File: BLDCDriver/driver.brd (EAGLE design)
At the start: 160 x 100 mm, 39 parts, among them Q1 NJM7800S, U1 QFN50P400X400X100-25NDRV8300D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, U2 AS5048A-HTSP-500, U4 SOP80P620X125-8N

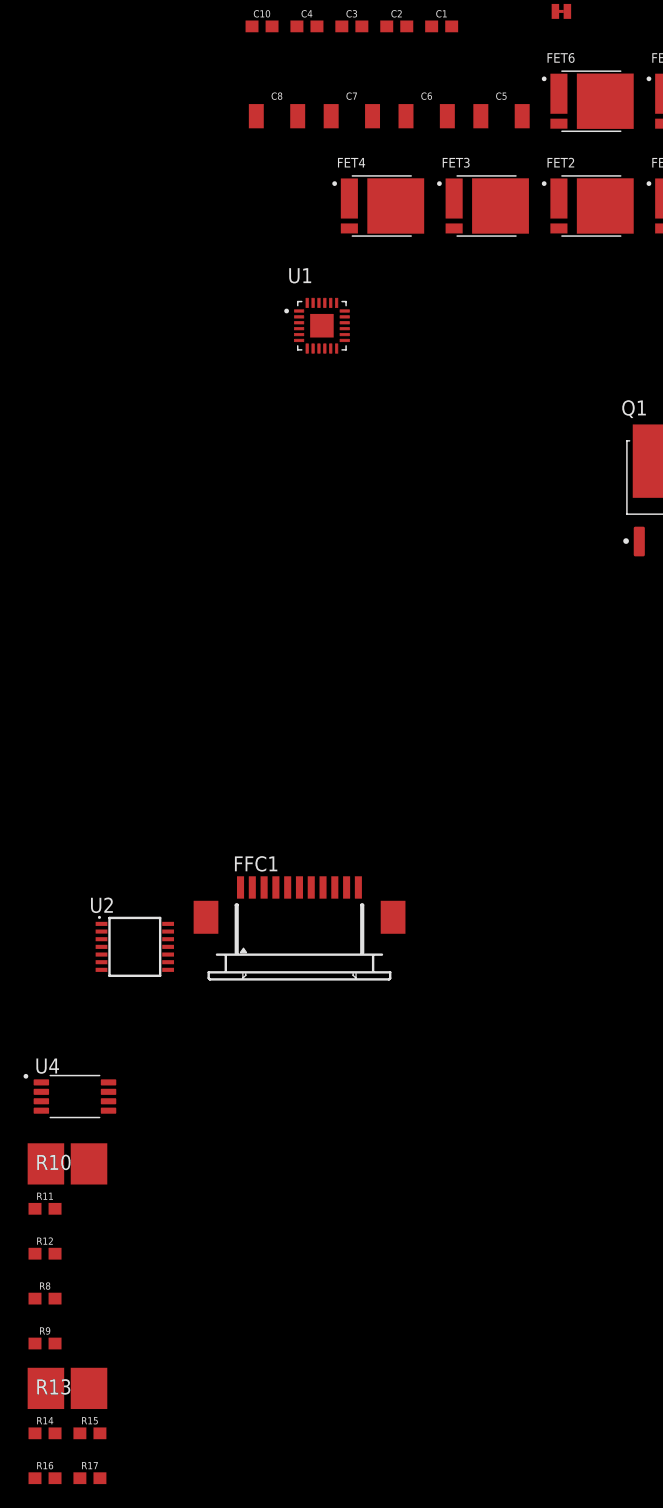
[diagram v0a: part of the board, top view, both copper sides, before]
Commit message: STM32と磁気エンコーダを追加した
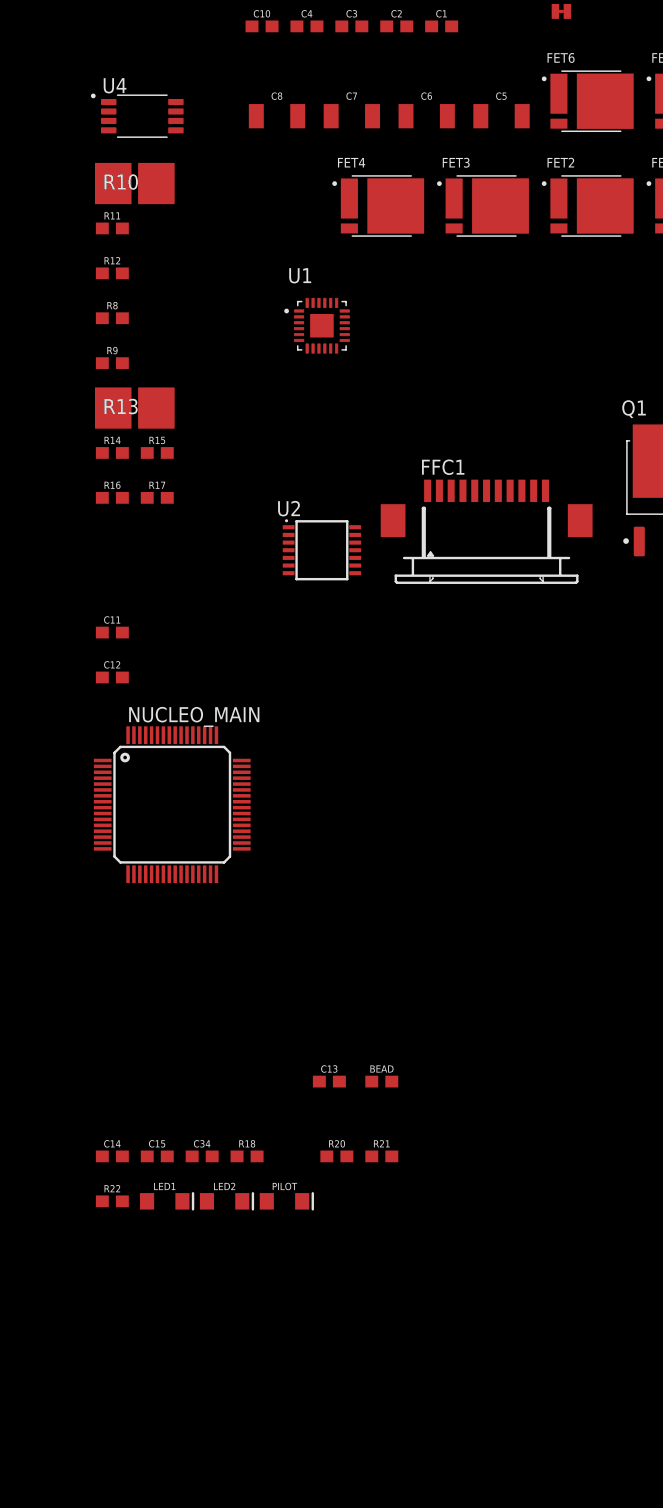
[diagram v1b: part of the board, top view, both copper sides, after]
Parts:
- added BEAD: 0, SparkFun-Resistors:0603
- added C11, C12, C15, C34: 0.1uF, SparkFun-Capacitors:0603
- added C13: 0.1UF_1608, Custom_Designed_By_Yusei:1608
- added C14: 4.7uF, SparkFun-Capacitors:0603
- added LED1, LED2, PILOT: (no value), Custom_Designed_By_Yusei:LED-1206
- added NUCLEO_MAIN: F446RET6, STM32F446RET6:STM32F446RET6
- added R18: 10k, Custom_Designed_By_Yusei:R0603
- added R20, R21, R22: 1k, Custom_Designed_By_Yusei:R0603
- moved R10 83.4 mm to (-64.1, 34.9)
- moved R11 83.4 mm to (-66.0, 31.1)
- moved R12 83.4 mm to (-66.0, 27.3)
- moved R13 83.4 mm to (-64.1, 15.9)
- moved R14 83.4 mm to (-66.0, 12.1)
- moved R15 83.4 mm to (-62.2, 12.1)
- moved R16 83.4 mm to (-66.0, 8.26)
- moved R17 83.4 mm to (-62.2, 8.26)
- moved R8 83.4 mm to (-66.0, 23.5)
- moved R9 83.4 mm to (-66.0, 19.7)
- moved U4 83.4 mm to (-63.5, 40.6)
- moved FFC1 37.2 mm to (-34.3, 6.35)
- moved U2 37.2 mm to (-48.3, 3.81)
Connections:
- removed net VDD3V: U2.12
- new net BALLRX: NUCLEO_MAIN.PA3
- new net BOOT0: NUCLEO_MAIN.BOOT0, R18.2
- new net BUTTON_CENTER: NUCLEO_MAIN.PC14
- new net BUTTON_LEFT: NUCLEO_MAIN.PC15
- new net BUTTON_RIGHT: NUCLEO_MAIN.PC13
- new net CLK: U2.2
- new net CS: U2.1
- new net LED1: LED1.A
- new net LED2: LED2.A
- new net LINE_A0: NUCLEO_MAIN.PB12
- new net LINE_A1: NUCLEO_MAIN.PB13
- new net MISO: U2.3
- new net MOSI: U2.4
- new net N$12: LED2.C, R21.1
- new net N$13: LED1.C, R22.1
- new net NRST: C13.1, NUCLEO_MAIN.NRST
- new net POWERLED_RESISTOR: PILOT.A, R20.1
- new net RGB_B: NUCLEO_MAIN.PA12
- new net RGB_G: NUCLEO_MAIN.PA8
- new net RGB_R: NUCLEO_MAIN.PC9
- new net SWCLK: NUCLEO_MAIN.PA14
- new net SWDIO: NUCLEO_MAIN.PA13
- new net VCAP: C14.1, NUCLEO_MAIN.VCAP_1
- new net VDDA: BEAD.1, NUCLEO_MAIN.VREF+
- net 3V3: now also BEAD.2, C11.1, C12.1, C15.1, C34.1, NUCLEO_MAIN.VBAT, NUCLEO_MAIN.VDD, NUCLEO_MAIN.VDD1, NUCLEO_MAIN.VDD2, NUCLEO_MAIN.VDD3, R20.2, U2.12
- net GND: now also C11.2, C12.2, C13.2, C14.2, C15.2, C34.2, NUCLEO_MAIN.VREF-, NUCLEO_MAIN.VSS, NUCLEO_MAIN.VSS1, NUCLEO_MAIN.VSS2, NUCLEO_MAIN.VSS3, PILOT.C, R18.1, R21.2, R22.2, U2.13

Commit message: somefix
# ==== Emojis ====
# ✨ :sparkles: Add new feature
# ✅  :white_check_mark: Update existing feature (not bug)
# ⚠️  :warning: Fix bug/error
# 🔥  :fire: Remove files or features
# ✏️ :pencil2: Fix typos
# 📝  :memo: Update documentation
# ♻️  :recycle: Dependencies update
# 🐧  :penguin: Improved the Linux
# 🍎  :apple: Improved the macOS
# 🔖 :bookmark: Add new library
# 🎉  :tada: Initial commit

# ==== Format ====
# :emoji: Subject
#
# Commit body...

# ==== Messages ====
# 新規(ファイル)機能追加: Add
# 機能修正、既存機能追加（バグではない): Update
# リファクタリング: Clean
# ファイル名変更:
# 削除など: Remove
# バグ修正: Fix
# バージョンアップ: Upgrade
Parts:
- added C16: 22UF-1210, SparkFun-Capacitors:1210
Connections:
- net GND: now also C16.1
- net GVDD: now also C16.2
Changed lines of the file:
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@@
 <attribute name="VALUE" x="-64.624" y="-17.7501" size="1.27" layer="27"/>
+</element>
+<element name="C16" library="SparkFun-Capacitors" package="1210" value="22UF-1210" x="-64.77" y="-55.88" smashed="yes">
+<attribute name="NAME" x="-64.77" y="-54.483" size="0.6096" layer="25" font="vector" ratio="20" align="bottom-center"/>
+<attribute name="VALUE" x="-64.77" y="-57.277" size="0.6096" layer="27" font="vector" ratio="20" align="top-center"/>
 </element>
 </elements>
@@
 <contactref element="Q1" pad="G"/>
 <contactref element="C4" pad="2"/>
-<contactref element="C8" pad="1"/>
-<contactref element="C9" pad="1"/>
 <contactref element="C10" pad="2"/>
 <contactref element="R7" pad="1"/>
@@
 <contactref element="NUCLEO_MAIN" pad="VSS"/>
 <contactref element="NUCLEO_MAIN" pad="VREF-"/>
+<contactref element="C8" pad="1"/>
+<contactref element="C9" pad="1"/>
+<contactref element="C16" pad="1"/>
+<wire x1="-65.19" y1="-51.435" x2="-66.525" y2="-55.88" width="0" layer="19" extent="1-1"/>
 <wire x1="-65.19" y1="-47.625" x2="-65.19" y2="-51.435" width="0" layer="19" extent="1-1"/>
 <wire x1="-61.38" y1="-47.625" x2="-65.19" y2="-47.625" width="0" layer="19" extent="1-1"/>
@@
 <contactref element="C8" pad="2"/>
 <contactref element="C9" pad="2"/>
-<wire x1="-28.448" y1="49.53" x2="-14.755" y2="49.53" width="0" layer="19" extent="1-1"/>
-<wire x1="-50.38" y1="48.26" x2="-28.448" y2="49.53" width="0" layer="19" extent="1-1"/>
-<wire x1="-50.315" y1="40.64" x2="-50.38" y2="48.26" width="0" layer="19" extent="1-1"/>
-<wire x1="-50.195" y1="22.61" x2="-50.315" y2="40.64" width="0" layer="19" extent="1-1"/>
-<wire x1="-16.77" y1="4.55" x2="-50.195" y2="22.61" width="0" layer="19" extent="1-1"/>
+<contactref element="C16" pad="2"/>
+<wire x1="-16.77" y1="4.55" x2="-63.015" y2="-55.88" width="0" layer="19" extent="1-1"/>
+<wire x1="-50.195" y1="22.61" x2="-16.77" y2="4.55" width="0" layer="19" extent="1-1"/>
+<wire x1="-50.315" y1="40.64" x2="-50.195" y2="22.61" width="0" layer="19" extent="1-1"/>
+<wire x1="-50.38" y1="48.26" x2="-50.315" y2="40.64" width="0" layer="19" extent="1-1"/>
+<wire x1="-28.448" y1="49.53" x2="-50.38" y2="48.26" width="0" layer="19" extent="1-1"/>
+<wire x1="-14.755" y1="49.53" x2="-28.448" y2="49.53" width="0" layer="19" extent="1-1"/>
 </signal>
 <signal name="DT">

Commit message: 自分、泣いていいすか
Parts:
- added C17: 0.1uF, Custom_Designed_By_Yusei:1608
- added C18: (no value), cap-pan40:E3,5-8
- added D1, D3, D4, D5, D6: WHITE, SparkFun-LED:LED-0603
- added D2: RED, SparkFun-LED:LED-0603
- added R19, R24, R25: 10k, SparkFun-Resistors:0603
- added R23, R26: 7k, SparkFun-Resistors:0603
- added R27: 8k, SparkFun-Resistors:0603
- added S1: SKRPACE010, Alps SW:SW_SKRPACE010
- added STLINK: MAIN, jst-xh:B6B-XH-A
- added U$2: BAT, BAT:BAT
- moved C16 144.1 mm to (25.4, 56.5)
- moved C14 141.7 mm to (40.0, 46.4)
- moved LED1 141.7 mm to (44.5, 42.5)
- moved LED2 141.7 mm to (49.5, 42.5)
- moved PILOT 141.7 mm to (54.6, 42.5)
- moved R22 141.7 mm to (40.0, 42.5)
- moved C15 141.7 mm to (43.8, 46.4)
- moved C34 141.7 mm to (47.6, 46.4)
- moved R18 141.7 mm to (51.4, 46.4)
- moved BEAD 119.6 mm to (45.1, 39.4)
- moved C13 119.6 mm to (40.6, 39.4)
- moved R20 119.6 mm to (41.3, 33.0)
- moved R21 119.6 mm to (45.1, 33.0)
- moved C11 106.2 mm to (38.1, 17.8)
- moved C12 106.2 mm to (38.1, 14.0)
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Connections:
- net BALLRX renamed USBRX
- removed net BUTTON_CENTER: NUCLEO_MAIN.PC14
- removed net BUTTON_LEFT: NUCLEO_MAIN.PC15
- removed net BUTTON_RIGHT: NUCLEO_MAIN.PC13
- removed net LINE_A0: NUCLEO_MAIN.PB12
- removed net LINE_A1: NUCLEO_MAIN.PB13
- removed net RGB_B: NUCLEO_MAIN.PA12
- removed net RGB_G: NUCLEO_MAIN.PA8
- removed net RGB_R: NUCLEO_MAIN.PC9
- new net C_U: NUCLEO_MAIN.PA0, R16.1, U4.1
- new net LED: NUCLEO_MAIN.PC14, R23.2
- new net N$14: D1.A, R19.1
- new net N$15: D2.A, R27.1
- new net N$16: D3.A, R24.1
- new net N$17: D4.A, R25.1
- new net N$18: D5.A, R26.1
- new net N$21: D6.A, R23.1
- new net SW: NUCLEO_MAIN.PC13, S1.2
- new net USBTX: NUCLEO_MAIN.PA2, STLINK.1
- net 3V3: now also C17.1, STLINK.5
- net CLK: now also NUCLEO_MAIN.PA5
- net CS: now also NUCLEO_MAIN.PB6
- net C_V: now also NUCLEO_MAIN.PA1; no longer R16.1, U4.1
- net GND: now also C17.2, C18.-, D1.C, D2.C, D3.C, D4.C, D5.C, D6.C, S1.4, STLINK.6, U$2.G
- net GVDD: now also R27.2
- net INA: now also NUCLEO_MAIN.PC7
- net INB: now also NUCLEO_MAIN.PB4
- net INC: now also NUCLEO_MAIN.PB10
- net MISO: now also NUCLEO_MAIN.PA6
- net MOSI: now also NUCLEO_MAIN.PA7
- net NRST: now also STLINK.2
- net PVDD: now also C18.+, R19.2, U$2.+
- net SWCLK: now also STLINK.4
- net SWDIO: now also STLINK.3
- net U: now also R13.2, R14.2, R24.2
- net U_CS: now also R13.1, R15.2
- net V: now also R25.2; no longer R13.2, R14.2
- net V_CS: no longer R13.1, R15.2
- net W: now also R26.2
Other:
- board size 160 x 100 mm -> 59 x 69.5 mm

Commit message: 救いはないんですか〜？
# ==== Emojis ====
# ✨ :sparkles: Add new feature
# ✅  :white_check_mark: Update existing feature (not bug)
# ⚠️  :warning: Fix bug/error
# 🔥  :fire: Remove files or features
# ✏️ :pencil2: Fix typos
# 📝  :memo: Update documentation
# ♻️  :recycle: Dependencies update
# 🐧  :penguin: Improved the Linux
# 🍎  :apple: Improved the macOS
# 🔖 :bookmark: Add new library
# 🎉  :tada: Initial commit

# ==== Format ====
# :emoji: Subject
#
# Commit body...

# ==== Messages ====
# 新規(ファイル)機能追加: Add
# 機能修正、既存機能追加（バグではない): Update
# リファクタリング: Clean
# ファイル名変更:
# 削除など: Remove
# バグ修正: Fix
# バージョンアップ: Upgrade
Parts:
- removed FET1, FET2, FET3, FET4, FET5, FET6: TPH11006NL, TPH11006NL:TRANS_TPHR8504PL,L1Q
- added Q2, Q3, Q4: SIZ240DT-T1-GE3, SIZ240DT-T1-GE3:TRANS_SIZ240DT-T1-GE3
- C2: value 0.1uF -> 22UF-1210; device SparkFun-Capacitors:0603 -> SparkFun-Capacitors:1210
- C7: value 22UF-1210 -> 0.1uF; device SparkFun-Capacitors:1210 -> SparkFun-Capacitors:0603
- moved C2 42.7 mm to (6.35, 50.2)
- moved R4 38.6 mm to (5.71, 45.7)
- moved R3 37.7 mm to (14.6, 50.8)
- moved C3 33.7 mm to (11.4, 46.4)
- moved C1 23.9 mm to (26.7, 40.0)
- moved R5 22.7 mm to (15.9, 38.1)
- moved R6 15.1 mm to (24.8, 38.7)
- moved C7 13.4 mm to (12.1, 38.1)
- moved C6 9.61 mm to (15.9, 47.0)
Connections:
- net BSTB: now also C3.1; no longer C2.1
- net BSTC: now also C7.1; no longer C3.1
- net GND: now also C2.1, Q2.5, Q2.6, Q2.7, Q3.5, Q3.6, Q3.7, Q4.5, Q4.6, Q4.7; no longer C7.1, FET2.1, FET4.1, FET6.1
- net N$1: now also Q3.1; no longer FET3.2
- net N$2: now also Q2.1; no longer FET1.2
- net N$4: now also Q2.8; no longer FET2.2
- net N$5: now also Q3.8; no longer FET4.2
- net N$6: now also Q4.1; no longer FET5.2
- net N$7: now also Q4.8; no longer FET6.2
- net PVDD: now also C2.2, Q2.10, Q2.2, Q2.3, Q2.4, Q3.10, Q3.2, Q3.3, Q3.4, Q4.10, Q4.2, Q4.3, Q4.4; no longer C7.2, FET1.3, FET3.3, FET5.3
- net U: now also Q2.9; no longer FET1.1, FET2.3
- net V: now also C3.2, Q3.9; no longer C2.2, FET3.1, FET4.3
- net W: now also C7.2, Q4.9; no longer C3.2, FET5.1, FET6.3

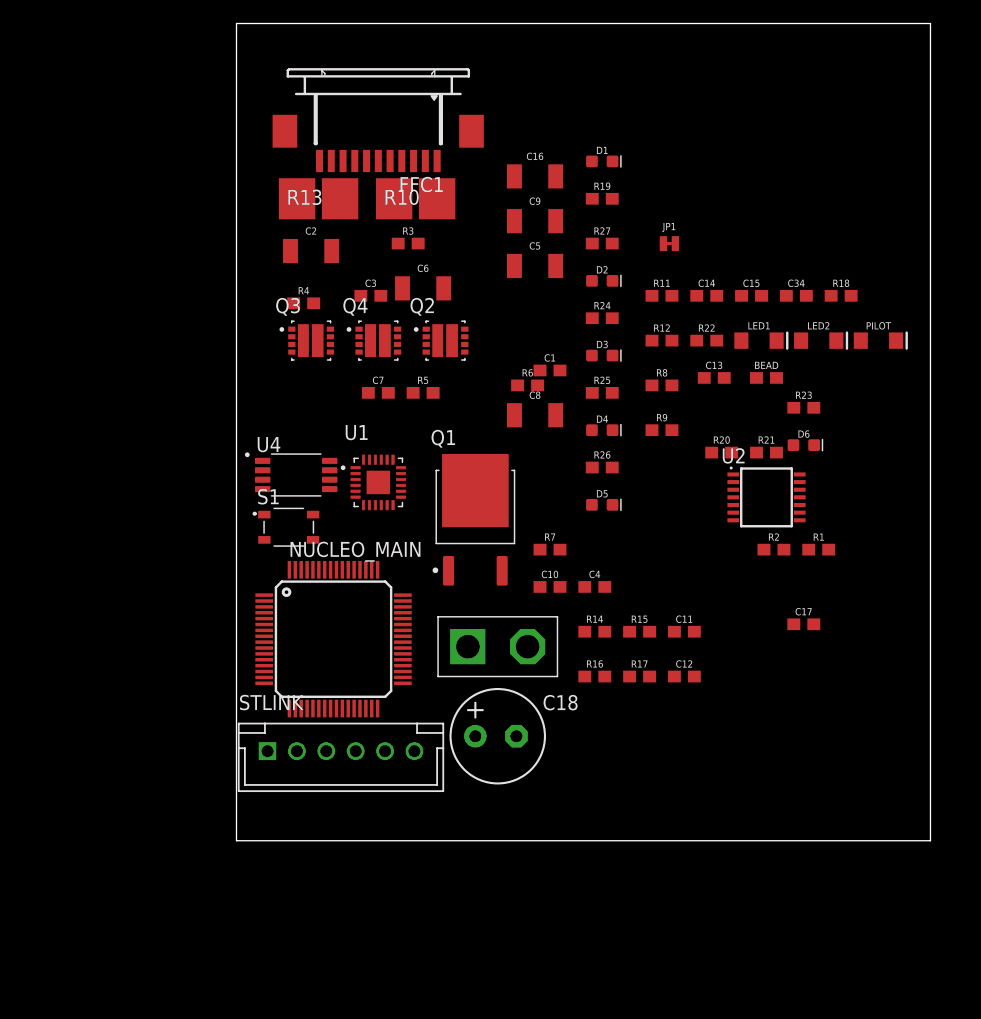
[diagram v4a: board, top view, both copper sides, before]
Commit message: ちょっと頑張った
# ==== Emojis ====
# ✨ :sparkles: Add new feature
# ✅  :white_check_mark: Update existing feature (not bug)
# ⚠️  :warning: Fix bug/error
# 🔥  :fire: Remove files or features
# ✏️ :pencil2: Fix typos
# 📝  :memo: Update documentation
# ♻️  :recycle: Dependencies update
# 🐧  :penguin: Improved the Linux
# 🍎  :apple: Improved the macOS
# 🔖 :bookmark: Add new library
# 🎉  :tada: Initial commit

# ==== Format ====
# :emoji: Subject
#
# Commit body...

# ==== Messages ====
# 新規(ファイル)機能追加: Add
# 機能修正、既存機能追加（バグではない): Update
# リファクタリング: Clean
# ファイル名変更:
# 削除など: Remove
# バグ修正: Fix
# バージョンアップ: Upgrade
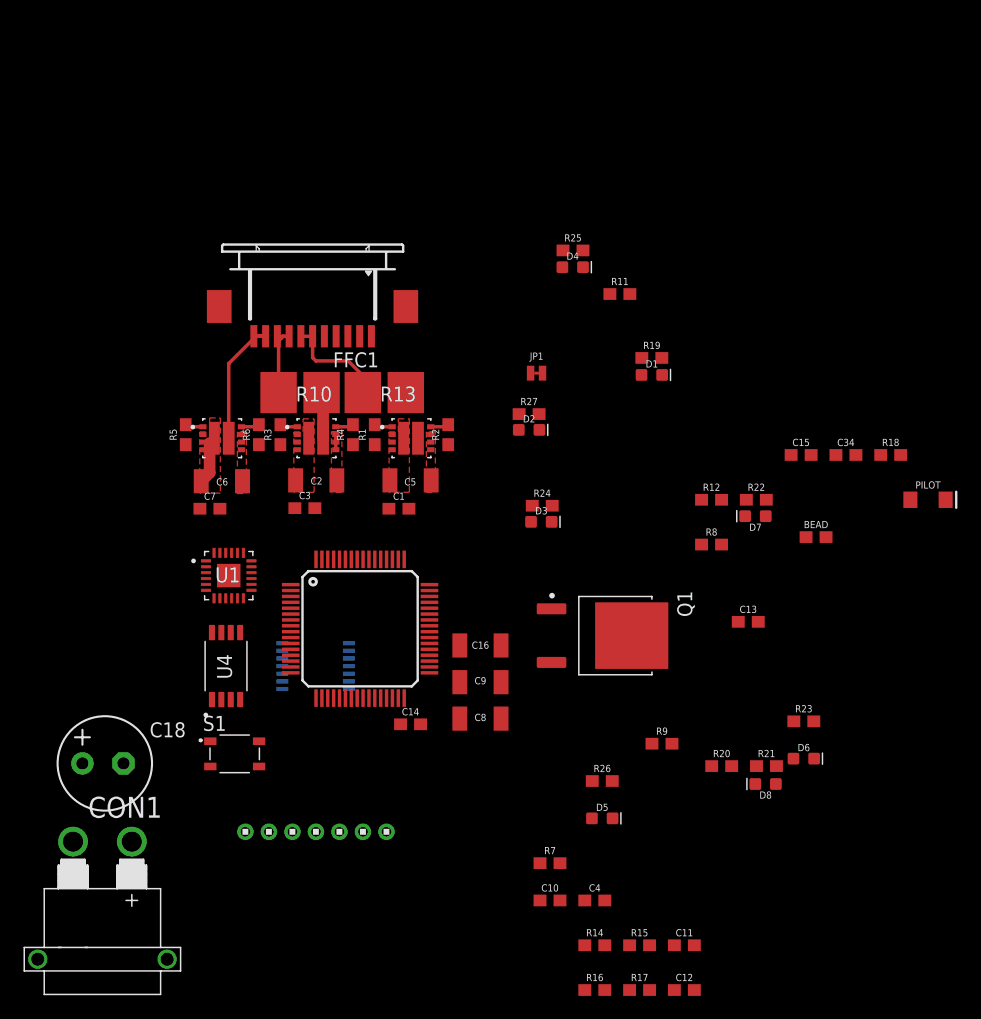
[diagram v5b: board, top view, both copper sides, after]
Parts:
- removed C17: 0.1uF, Custom_Designed_By_Yusei:1608
- removed LED1, LED2: (no value), Custom_Designed_By_Yusei:LED-1206
- removed STLINK: MAIN, jst-xh:B6B-XH-A
- added CON1: XT30PW-M, XTn0 amass:XT30PW-M
- added D7, D8: WHITE, SparkFun-LED:LED-0603
- U$2: value BAT -> 1X7; device BAT:BAT -> headers(2mm):1X7
- moved C14 44.3 mm to (14.8, 9.91)
- moved U2 41.0 mm to (6.73, 14.9), flipped to the bottom
- moved C16 40.2 mm to (20.8, 16.6)
- moved C9 39.5 mm to (20.8, 13.5)
- moved R1 39.0 mm to (11.8, 34.5), turned to 90 degrees
- moved C18 33.5 mm to (-11.2, 6.58)
- moved R2 29.4 mm to (18.0, 34.5), turned to 90 degrees
- moved C10 26.7 mm to (26.7, -5.08)
- moved C11 26.7 mm to (38.1, -8.89)
- moved C12 26.7 mm to (38.1, -12.7)
- moved C4 26.7 mm to (30.5, -5.08)
- moved D6 26.7 mm to (48.3, 6.99)
- moved R14 26.7 mm to (30.5, -8.89)
- moved R15 26.7 mm to (34.3, -8.89)
- moved R16 26.7 mm to (30.5, -12.7)
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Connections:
- net N$1 renamed HB
- net N$2 renamed HA
- net N$4 renamed LA
- net N$5 renamed LB
- net N$6 renamed HC
- net N$7 renamed LC
- net 3V3: now also U$2.2; no longer C17.1, STLINK.5
- net GND: now also CON1.-, U$2.1; no longer C17.2, STLINK.6, U$2.G
- net LED1: now also D7.A; no longer LED1.A
- net LED2: now also D8.A; no longer LED2.A
- net N$12: now also D8.C; no longer LED2.C
- net N$13: now also D7.C; no longer LED1.C
- net NRST: now also U$2.5; no longer STLINK.2
- net PVDD: now also CON1.+; no longer U$2.+
- net SWCLK: now also U$2.3; no longer STLINK.4
- net SWDIO: now also U$2.4; no longer STLINK.3
- net USBRX: now also U$2.7
- net USBTX: now also U$2.6; no longer STLINK.1
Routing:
- net W: track 0.00 -> 11.5 mm
- net U_CS: track 0.00 -> 9.16 mm
- net V_CS: track 0.00 -> 5.96 mm
- net V: track 0.00 -> 4.01 mm
- net PVDD: track 0.00 -> 3.55 mm
- net LA: track 0.00 -> 1.56 mm
- net HA: track 0.00 -> 1.56 mm
- net LC: track 0.00 -> 1.56 mm
- net HC: track 0.00 -> 1.53 mm
- net LB: track 0.00 -> 1.53 mm
- net HB: track 0.00 -> 1.51 mm
- net GND: track 0.00 -> 1.43 mm
- added copper zone on layer 1, net GND
- added copper zone on layer 1, net PVDD
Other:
- board outline removed

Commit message: いい感じの配置アイディアが降ってきた
- 裏側にも実装する
- 20V非対応にする(GVDD別供給にも対応)
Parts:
- moved C16 15.4 mm to (7.01, 23.6)
- moved C9 15.3 mm to (7.11, 20.3)
- moved C8 15.2 mm to (7.11, 17.1)
- moved NUCLEO_MAIN 7.95 mm to (18.4, 18.6), flipped to the bottom
- moved C6 3.53 mm to (-1.27, 34.1), flipped to the bottom, turned to 0 degrees
- moved CON1 2.06 mm to (-9.78, -1.35)
- flipped C2 to the bottom, turned to 0 degrees
- flipped C5 to the bottom, turned to 0 degrees
- turned Q1 to 0 degrees
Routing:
- net PVDD: track 3.55 -> 0.00 mm
